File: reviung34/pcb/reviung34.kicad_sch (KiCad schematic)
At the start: 80 parts, among them SW1 SW_PUSH, SW10 SW_PUSH, SW11 SW_PUSH, SW12 SW_PUSH, SW13 SW_PUSH, SW14 SW_PUSH, SW15 SW_PUSH, SW16 SW_PUSH, SW17 SW_PUSH, SW18 SW_PUSH, SW19 SW_PUSH, SW2 SW_PUSH, SW20 SW_PUSH, SW21 SW_PUSH, SW22 SW_PUSH, SW23 SW_PUSH, SW24 SW_PUSH, SW25 SW_PUSH, SW26 SW_PUSH, SW27 SW_PUSH, SW28 SW_PUSH, SW29 SW_PUSH, SW3 SW_PUSH, SW30 SW_PUSH, SW31 SW_PUSH, SW32 SW_PUSH, SW33 SW_PUSH, SW34 SW_PUSH, SW35 SW_PUSH, SW4 SW_PUSH, SW5 SW_PUSH, SW6 SW_PUSH, SW7 SW_PUSH, SW8 SW_PUSH, SW9 SW_PUSH, U1 ProMicro

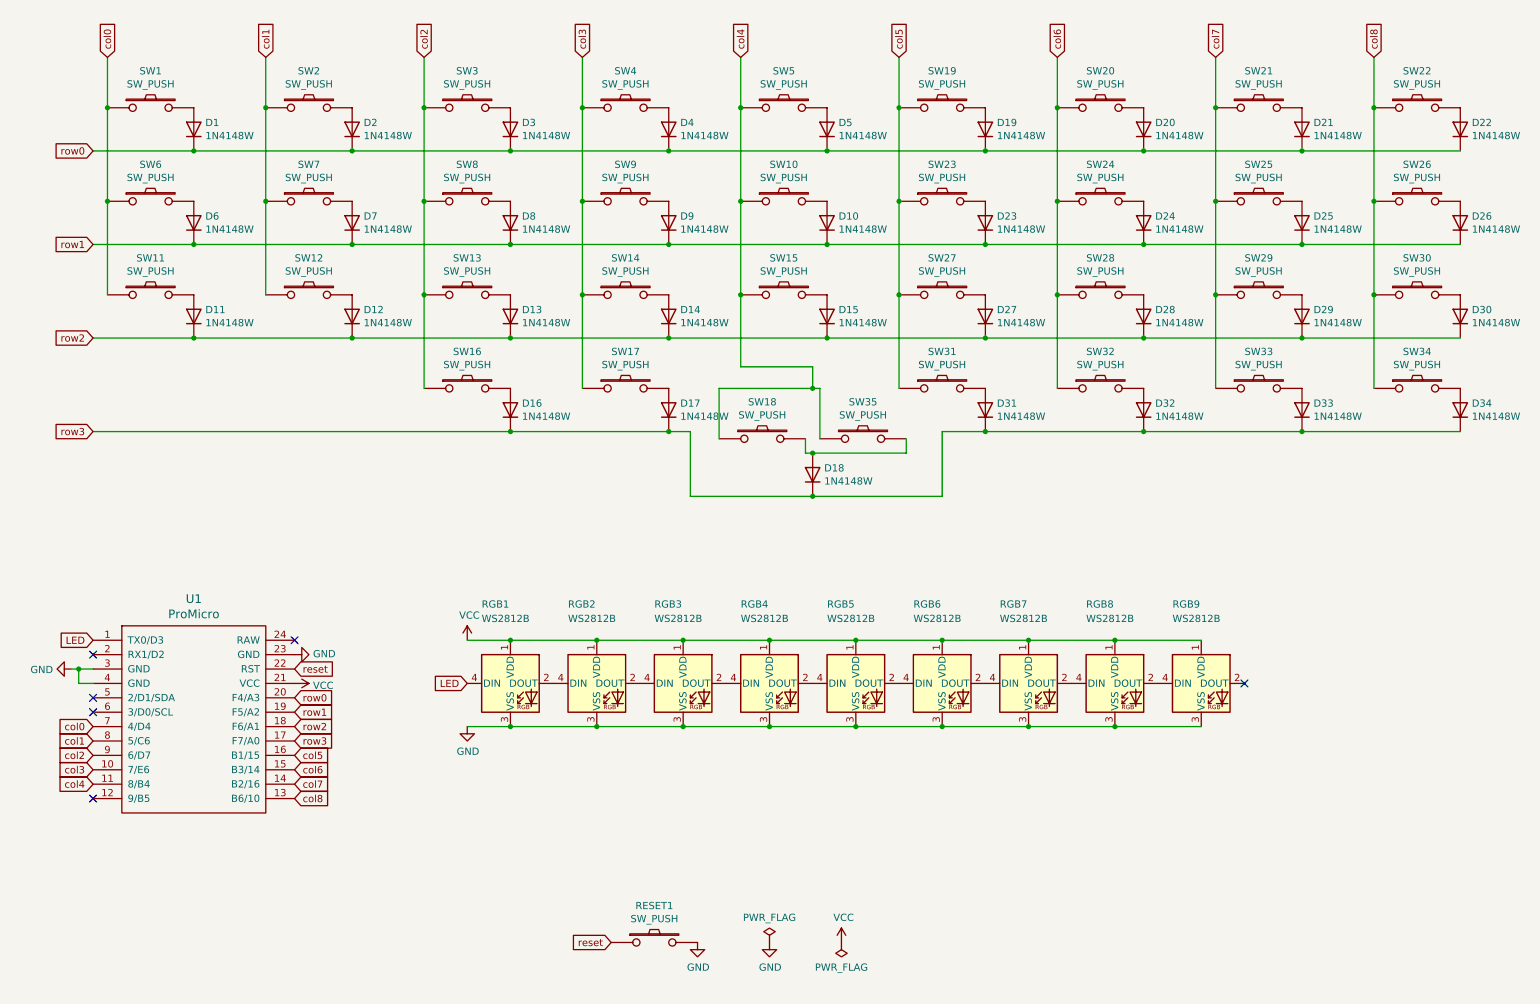
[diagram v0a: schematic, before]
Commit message: reviung34: circuit updates
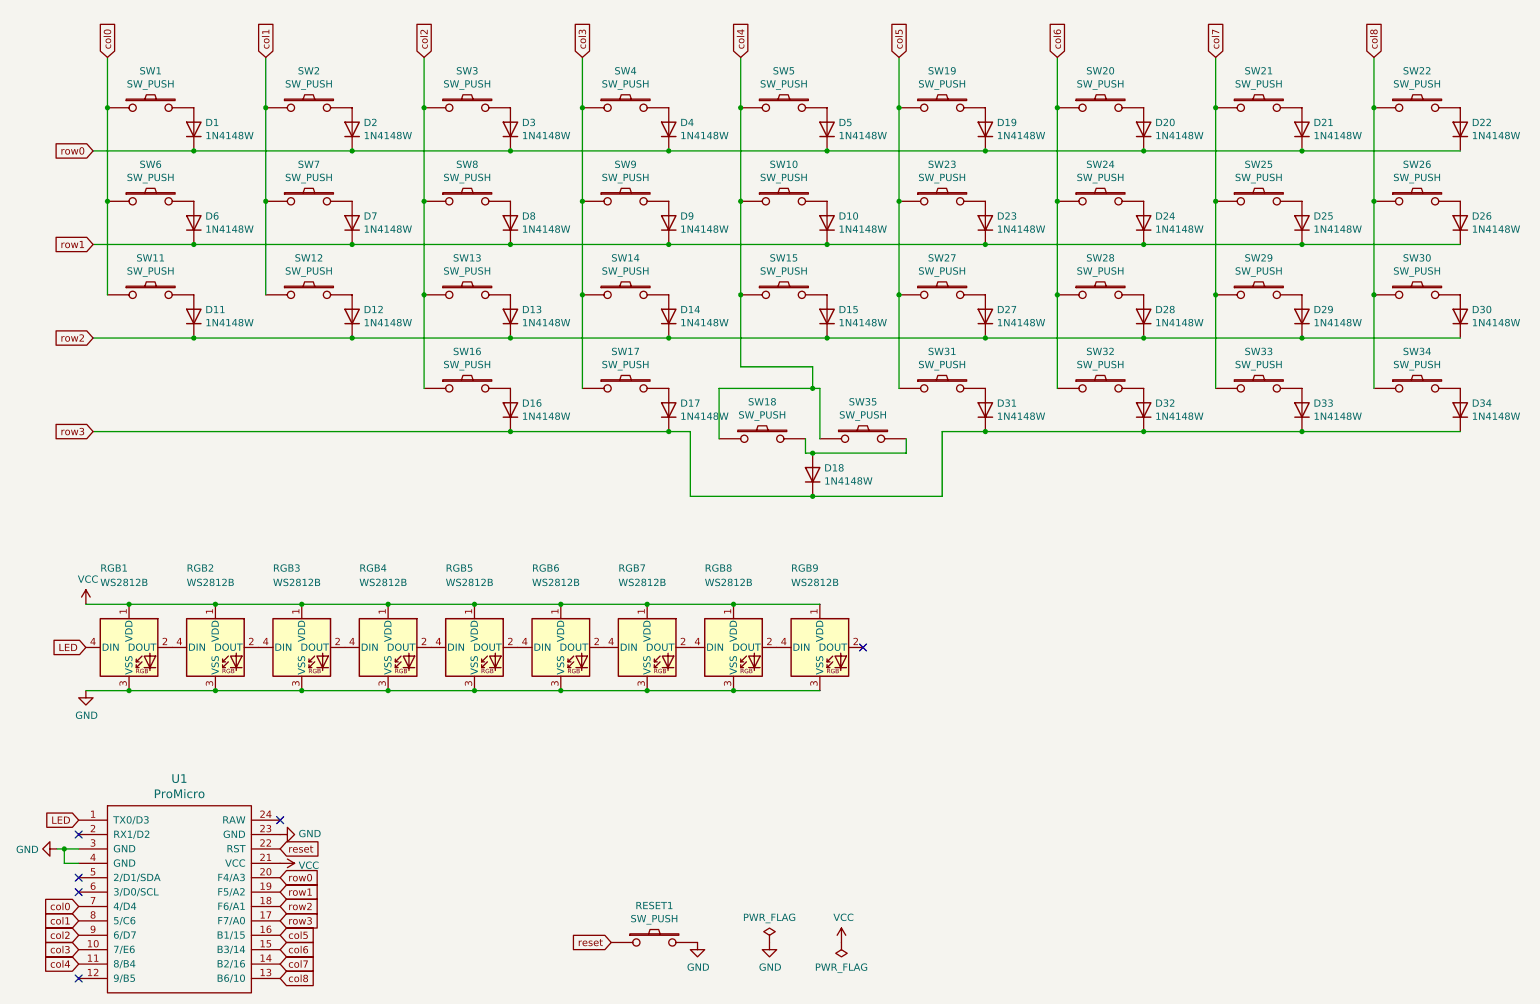
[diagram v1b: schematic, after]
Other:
- title: REVIUNG34 -> REVIUNG34 Hotswap
- moved on the sheet: RGB1, RGB2, RGB3, RGB4, RGB5, RGB6, RGB7, RGB8, RGB9, U1
